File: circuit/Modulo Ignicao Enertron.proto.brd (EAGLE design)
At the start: 72.9 x 58.5 mm, 36 parts, among them IC1 PIC12F675P, IC2 78L05, K1 ISP, P1 5k, Q1 IRGB14C40L

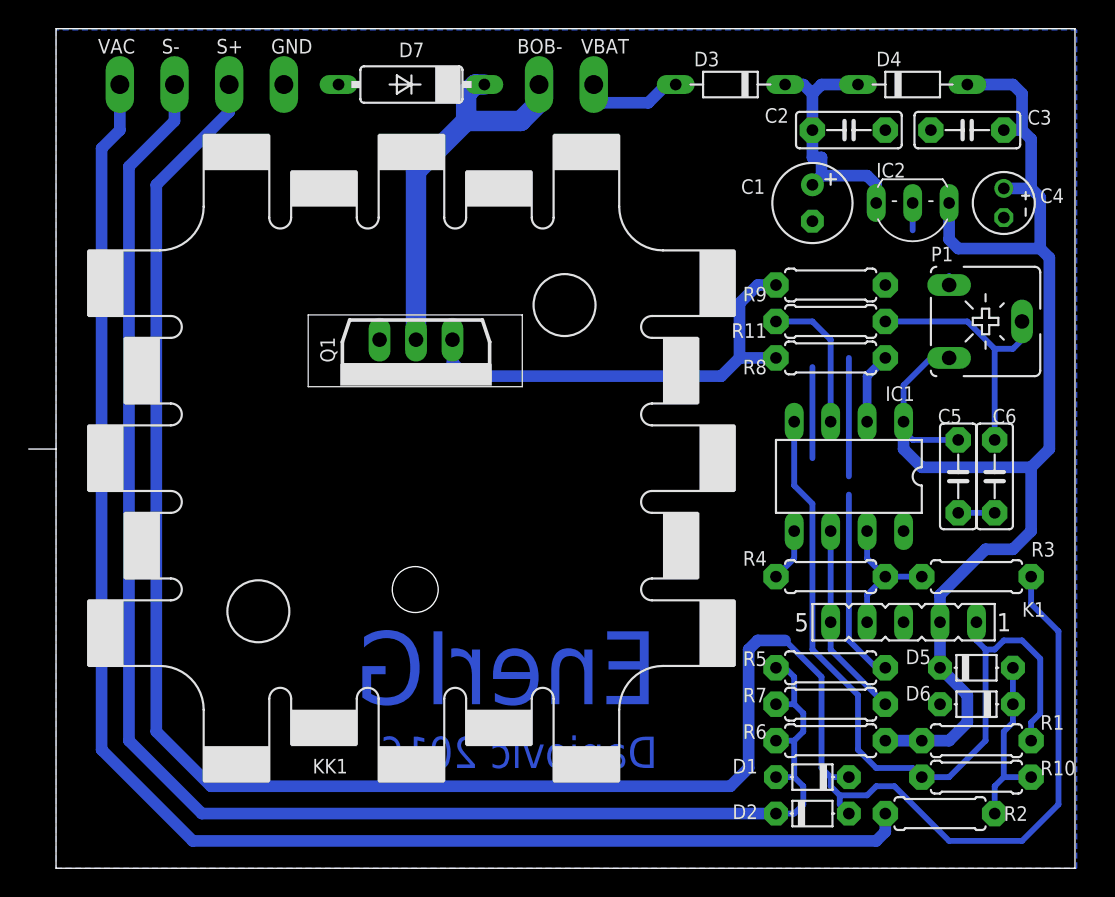
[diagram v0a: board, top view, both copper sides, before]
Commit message: Corrected circuit around MCLR
Corrected circuit around MCLR pin to allow ICSP. The diode network was
bypassing MCLR high voltage to VCC. A series resistor fixed the problem.
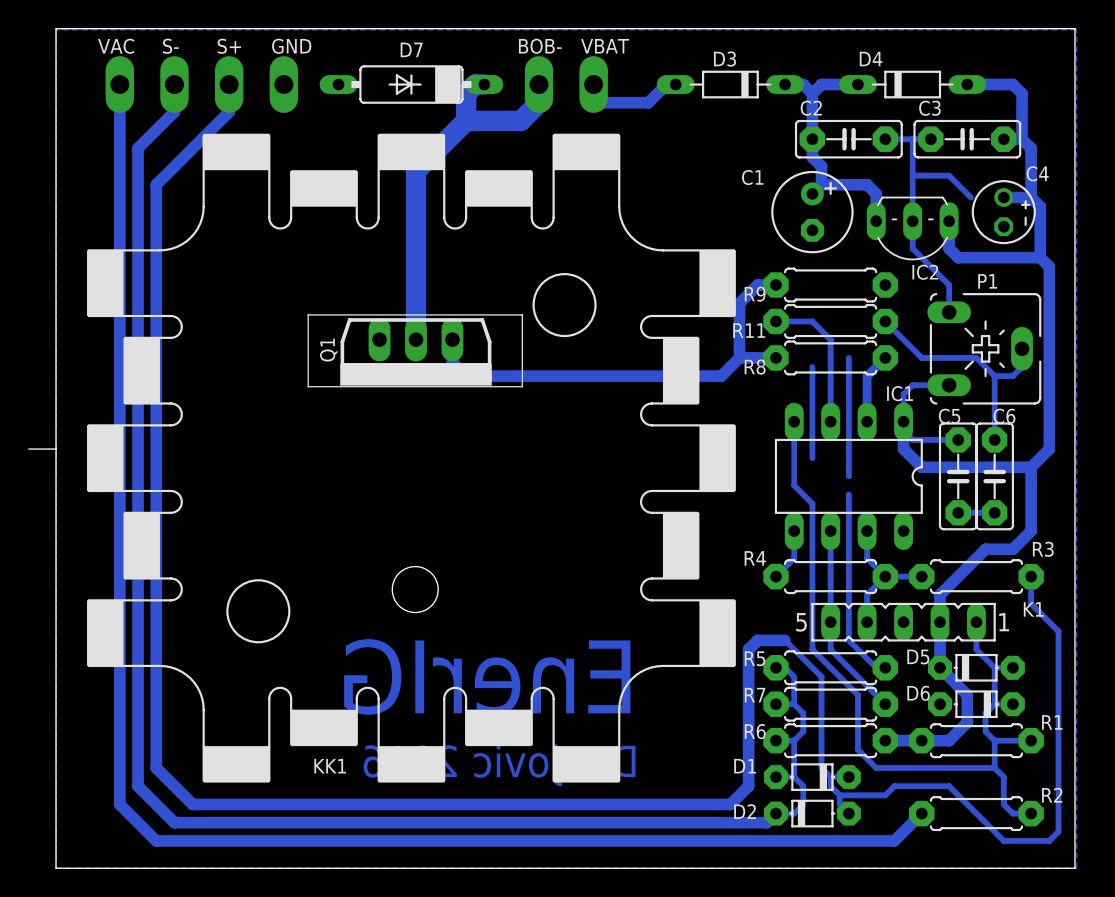
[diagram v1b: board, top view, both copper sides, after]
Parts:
- removed R10: 4k7, rcl:0207/7L
- R1: value 47k -> 10k
- moved R2 2.54 mm to (64.8, 3.81)
- moved P1 1.91 mm to (65.4, 36.2)
- moved IC2 1.27 mm to (60.3, 45.1)
- moved C2 0.64 mm to (55.9, 50.8)
- moved C3 0.64 mm to (64.1, 50.8)
- moved C1 0.63 mm to (53.3, 45.7)
- moved C4 0.63 mm to (66.7, 45.7)
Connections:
- removed net N$4: D5.A, D6.C, R10.3, R2.3
- net !MCLR: now also D5.A, D6.C, R2.3; no longer R10.4
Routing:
- net GND: track 33.2 -> 51.6 mm
- net N$4: track 12.6 -> 0.00 mm
- net N$5: track 151.6 -> 156.0 mm
- net N$11: track 105.7 -> 107.9 mm
- net +5V: track 94.2 -> 92.4 mm
- net N$2: track 111.4 -> 112.9 mm
- net !MCLR: track 54.5 -> 56.0 mm
- net N$9: track 18.2 -> 17.1 mm
- net N$1: track 18.2 -> 19.1 mm
